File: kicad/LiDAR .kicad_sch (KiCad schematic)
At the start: 6 parts, among them J17 LiDAR, Q20 AO3400

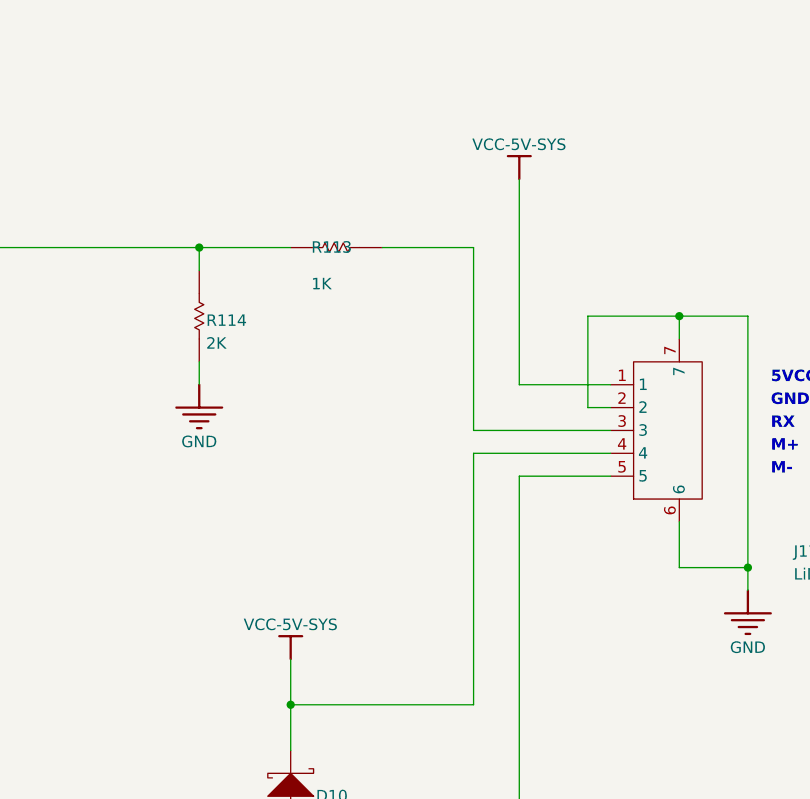
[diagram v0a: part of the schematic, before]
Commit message: Added Pi CM4/CM5
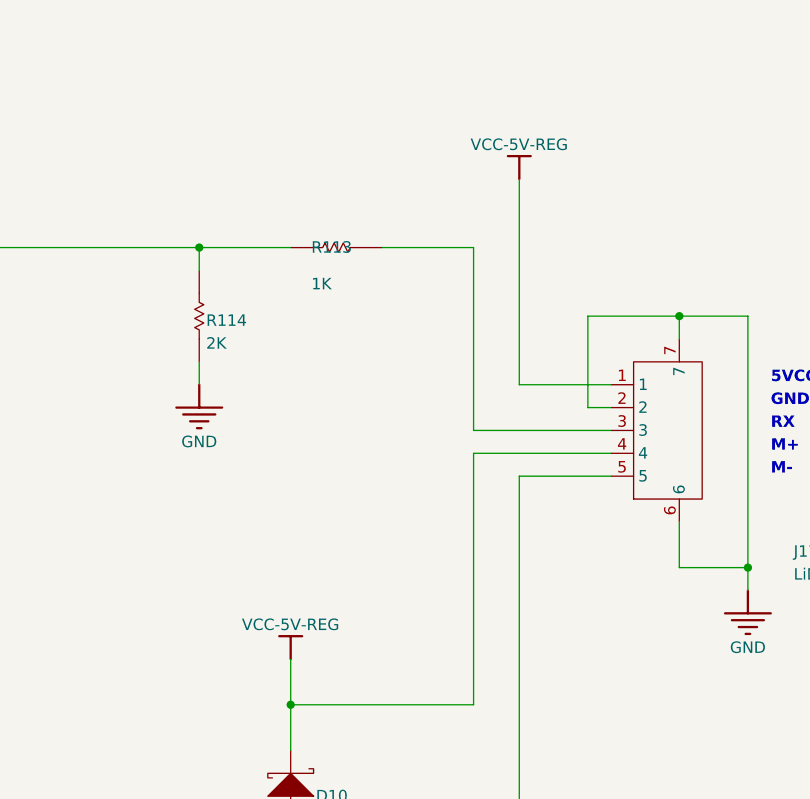
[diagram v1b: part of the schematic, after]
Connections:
- net VCC-5V-SYS renamed VCC-5V-REG
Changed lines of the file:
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@@
-	)
-	(symbol
-		(lib_id "oomwoo-kicad-altium-import:VCC-5V-SYS_BAR")
-		(at 329.565 133.985 180)
-		(unit 1)
-		(body_style 1)
-		(exclude_from_sim no)
-		(in_bom yes)
-		(on_board yes)
-		(in_pos_files yes)
-		(dnp no)
-		(property "Reference" "#PWR0604"
-			(at 329.565 133.985 0)
-			(hide yes)
-			(show_name no)
-			(do_not_autoplace no)
-			(effects
-				(font
-					(size 1.27 1.27)
-				)
-			)
-		)
-		(property "Value" "VCC-5V-SYS"
-			(at 329.565 130.175 0)
-			(show_name no)
-			(do_not_autoplace no)
-			(effects
-				(font
-					(size 1.27 1.27)
-				)
-			)
-		)
-		(property "Footprint" ""
-			(at 329.565 133.985 0)
-			(show_name no)
-			(do_not_autoplace no)
-			(effects
-				(font
-					(size 1.27 1.27)
-				)
-			)
-		)
-		(property "Datasheet" ""
-			(at 329.565 133.985 0)
-			(show_name no)
-			(do_not_autoplace no)
-			(effects
-				(font
-					(size 1.27 1.27)
-				)
-			)
-		)
-		(property "Description" ""
-			(at 329.565 133.985 0)
-			(show_name no)
-			(do_not_autoplace no)
-			(effects
-				(font
-					(size 1.27 1.27)
-				)
-			)
-		)
-		(pin ""
-		)
-		(instances
-			(project "oomwoo-kicad"
-				(path "/dbcfb655-8d45-4808-9a74-2a0eb03372e8/994d55da-8e8c-4fe8-9877-f2e4533982e7"
-					(reference "#PWR0604")
-					(unit 1)
-				)
-			)
-		)
 	)
 	(symbol
@@
 	)
 	(symbol
-		(lib_id "oomwoo-kicad-altium-import:VCC-5V-SYS_BAR")
-		(at 304.165 187.325 180)
-		(unit 1)
-		(body_style 1)
-		(exclude_from_sim no)
-		(in_bom yes)
-		(on_board yes)
-		(in_pos_files yes)
-		(dnp no)
-		(property "Reference" "#PWR0602"
-			(at 304.165 187.325 0)
-			(hide yes)
-			(show_name no)
-			(do_not_autoplace no)
-			(effects
-				(font
-					(size 1.27 1.27)
-				)
-			)
-		)
-		(property "Value" "VCC-5V-SYS"
-			(at 304.165 183.515 0)
-			(show_name no)
-			(do_not_autoplace no)
-			(effects
-				(font
-					(size 1.27 1.27)
-				)
-			)
-		)
-		(property "Footprint" ""
-			(at 304.165 187.325 0)
-			(show_name no)
-			(do_not_autoplace no)
-			(effects
-				(font
-					(size 1.27 1.27)
-				)
-			)
-		)
-		(property "Datasheet" ""
-			(at 304.165 187.325 0)
-			(show_name no)
-			(do_not_autoplace no)
-			(effects
-				(font
-					(size 1.27 1.27)
-				)
-			)
-		)
-		(property "Description" ""
-			(at 304.165 187.325 0)
-			(show_name no)
-			(do_not_autoplace no)
-			(effects
-				(font
-					(size 1.27 1.27)
-				)
-			)
-		)
-		(pin ""
-		)
-		(instances
-			(project "oomwoo-kicad"
-				(path "/dbcfb655-8d45-4808-9a74-2a0eb03372e8/994d55da-8e8c-4fe8-9877-f2e4533982e7"
-					(reference "#PWR0602")
-					(unit 1)
-				)
-			)
-		)
-	)
-	(symbol
 		(lib_id "DesignLibrary:LiDAR_1_Resistor-1_DesignLibrary.SchLib")
 		(at 294.005 154.305 180)
@@
 				(path "/dbcfb655-8d45-4808-9a74-2a0eb03372e8/994d55da-8e8c-4fe8-9877-f2e4533982e7"
 					(reference "R114")
+					(unit 1)
+				)
+			)
+		)
+	)
+	(symbol
+		(lib_id "oomwoo-kicad-altium-import:VCC-5V-REG_BAR")
+		(at 329.565 133.985 180)
+		(unit 1)
+		(body_style 1)
+		(exclude_from_sim no)
+		(in_bom yes)
+		(on_board yes)
+		(in_pos_files yes)
+		(dnp no)
+		(property "Reference" "#PWR070"
+			(at 329.565 133.985 0)
+			(hide yes)
+			(show_name no)
+			(do_not_autoplace no)
+			(effects
+				(font
+					(size 1.27 1.27)
+				)
+			)
+		)
+		(property "Value" "VCC-5V-REG"
+			(at 329.565 130.175 0)
+			(show_name no)
+			(do_not_autoplace no)
+			(effects
+				(font
+					(size 1.27 1.27)
+				)
+			)
+		)
+		(property "Footprint" ""
+			(at 329.565 133.985 0)
+			(show_name no)
+			(do_not_autoplace no)
+			(effects
+				(font
+					(size 1.27 1.27)
+				)
+			)
+		)
+		(property "Datasheet" ""
+			(at 329.565 133.985 0)
+			(show_name no)
+			(do_not_autoplace no)
+			(effects
+				(font
+					(size 1.27 1.27)
+				)
+			)
+		)
+		(property "Description" ""
+			(at 329.565 133.985 0)
+			(show_name no)
+			(do_not_autoplace no)
+			(effects
+				(font
+					(size 1.27 1.27)
+				)
+			)
+		)
+		(pin ""
+		)
+		(instances
+			(project "oomwoo-kicad"
+				(path "/dbcfb655-8d45-4808-9a74-2a0eb03372e8/994d55da-8e8c-4fe8-9877-f2e4533982e7"
+					(reference "#PWR070")
 					(unit 1)
 				)
@@
 					(unit 1)
 				)
+			)
+		)
+	)
+	(symbol
+		(lib_id "oomwoo-kicad-altium-import:VCC-5V-REG_BAR")
+		(at 304.165 187.325 180)
+		(unit 1)
+		(body_style 1)
+		(exclude_from_sim no)
+		(in_bom yes)
+		(on_board yes)
+		(in_pos_files yes)
+		(dnp no)
+		(property "Reference" "#PWR071"
+			(at 304.165 187.325 0)
+			(hide yes)
+			(show_name no)
+			(do_not_autoplace no)
+			(effects
+				(font
+					(size 1.27 1.27)
+				)
+			)
+		)
+		(property "Value" "VCC-5V-REG"
+			(at 304.165 183.515 0)
+			(show_name no)
+			(do_not_autoplace no)
+			(effects
+				(font
+					(size 1.27 1.27)
+				)
+			)
+		)
+		(property "Footprint" ""
+			(at 304.165 187.325 0)
+			(show_name no)
+			(do_not_autoplace no)
+			(effects
+				(font
+					(size 1.27 1.27)
+				)
+			)
+		)
+		(property "Datasheet" ""
+			(at 304.165 187.325 0)
+			(show_name no)
+			(do_not_autoplace no)
+			(effects
+				(font
+					(size 1.27 1.27)
+				)
+			)
+		)
+		(property "Description" ""
+			(at 304.165 187.325 0)
+			(show_name no)
+			(do_not_autoplace no)
+			(effects
+				(font
+					(size 1.27 1.27)
+				)
+			)
+		)
+		(pin ""
+		)
+		(instances
+			(project "oomwoo-kicad"
+				(path "/dbcfb655-8d45-4808-9a74-2a0eb03372e8/994d55da-8e8c-4fe8-9877-f2e4533982e7"
+					(reference "#PWR071")
+					(unit 1)
+				)

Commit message: Changed MCU to STM32G473VCT6
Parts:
- R113, R114, R116: footprint oomwoo_altium:RES-0402 -> Resistor_SMD:R_0603_1608Metric
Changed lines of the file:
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@@
 			)
 		)
-		(property "Footprint" "oomwoo_altium:RES-0402"
+		(property "Footprint" "Resistor_SMD:R_0603_1608Metric"
 			(at 281.305 235.585 0)
 			(hide yes)
@@
 			)
 		)
-		(property "Footprint" "oomwoo_altium:RES-0402"
+		(property "Footprint" "Resistor_SMD:R_0603_1608Metric"
 			(at 294.005 154.305 0)
 			(hide yes)
@@
 			)
 		)
-		(property "Footprint" "oomwoo_altium:RES-0402"
+		(property "Footprint" "Resistor_SMD:R_0603_1608Metric"
 			(at 304.165 141.605 0)
 			(hide yes)

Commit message: STM32G473VCT6
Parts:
- removed J17: LiDAR, oomwoo_altium:CONN-SMD_5P-P1.25_XUNPU_WAFER-GH1.25-5PWB, symbol DesignLibrary:LiDAR_0_HDRx5_DesignLibrary.SchLib
- removed R113: 1K, Resistor_SMD:R_0603_1608Metric, symbol DesignLibrary:LiDAR_0_Resistor-1_DesignLibrary.SchLib
- removed R114: 2K, Resistor_SMD:R_0603_1608Metric, symbol DesignLibrary:LiDAR_1_Resistor-1_DesignLibrary.SchLib
- added C18, C39: 100nF/10V, Capacitor_SMD:C_0603_1608Metric, symbol Device:C_Small
- added LIDAR1: WAFER-GH1_25-6PWB, JLCImport:WAFER-GH1_25-6PWB, symbol JLCImport:WAFER-GH1_25-6PWB
- added U2: TXU0202DCUR, JLCImport:TXU0202DCUR, symbol JLCImport:TXU0202DCUR
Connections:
- net GND: now also C18.2, C39.2, LIDAR1.2, LIDAR1.7, LIDAR1.8, U2.2 (GND)
- net LiDAR-RXD: now also U2.8 (B1Y)
- net VCC-5V-REG: now also C18.1, LIDAR1.1, LIDAR1.5, U2.3 (VCCA)
- net at D10.1 (A), Q20.3 (D): now also LIDAR1.6
- new net: LIDAR1.3, U2.5 (A1)
- new net: LIDAR1.4, U2.4 (A2Y)
- new net LiDAR-TXD: U2.1 (B2)
- new net VCC-3V3-P: C39.1, U2.6 (OE), U2.7 (VCCB)
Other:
- note added: "LIDAR_RX"
- note added: "LIDAR_TX"
- note added: "VCC"
- note removed: "5VCC"
- note removed: "RX"

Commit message: External RTC; IR light; side sensors
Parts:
- removed C18, C39: 100nF/10V, Capacitor_SMD:C_0603_1608Metric, symbol Device:C_Small
- removed U2: TXU0202DCUR, JLCImport:TXU0202DCUR, symbol JLCImport:TXU0202DCUR
- added R47: 10kOhm, Resistor_SMD:R_0603_1608Metric_Pad0.98x0.95mm_HandSolder, symbol Device:R_US
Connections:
- net LiDAR-RXD: now also R47.1
- net LiDAR-TXD: now also LIDAR1.4
- net at LIDAR1.3: now also R47.2
